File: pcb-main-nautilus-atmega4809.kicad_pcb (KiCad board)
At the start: 4 copper layers, 68.6 x 53.3 mm, 91 parts, among them J1 694106301002, J2 105017-0001, J3 FTSH-105-01-L-DV-007-K, J4 75844-101-06LF, J5 66951-006LF, J6 66951-010LF, J7 66951-008LF, J8 66951-008LF, Q1 BSS138PW, Q2 BSS138PW, Q3 BSS138PW, SW1 PTS645SH43SMTR92 LFS, U1 NCP1117-5.0_TO252, U2 AP2112K-3.3, U3 ATSAMD11D14A-SS, U4 ATmega4809-A

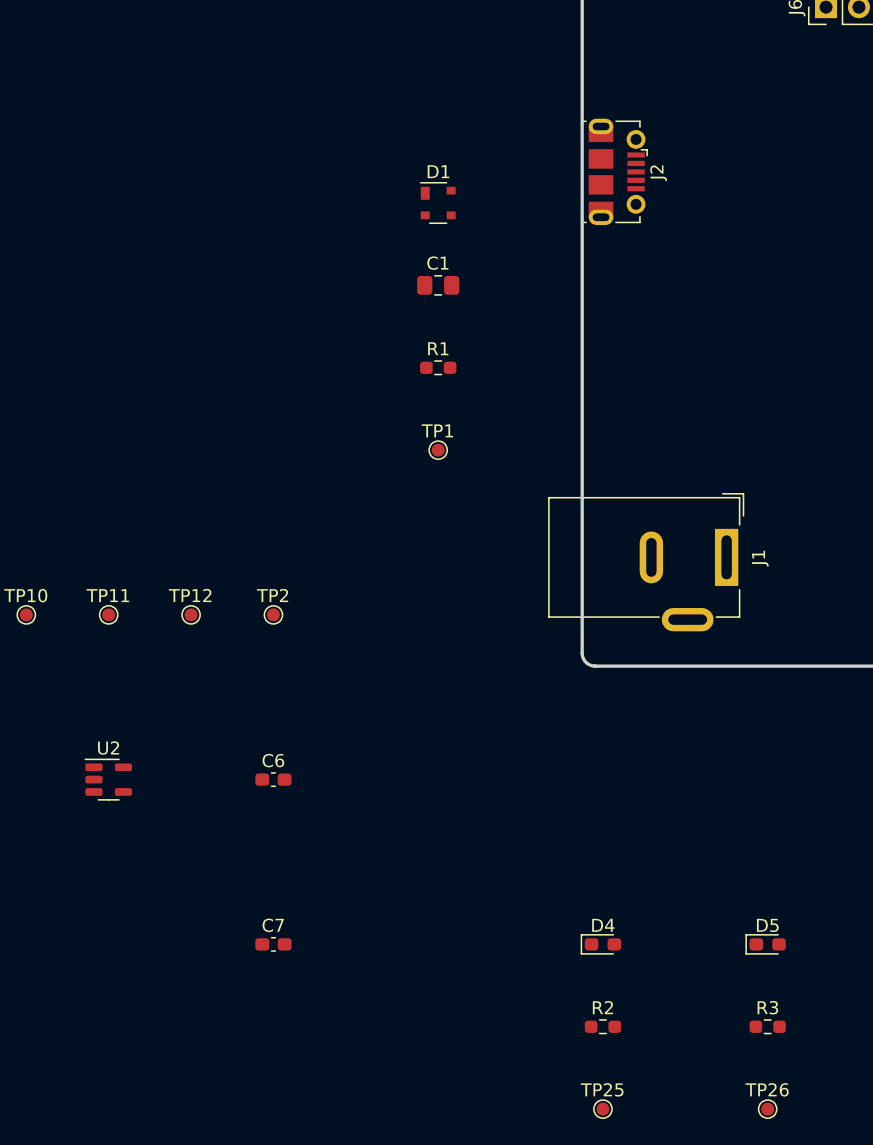
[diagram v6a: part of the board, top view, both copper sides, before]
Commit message: Arrange power indicators
Supports #4.
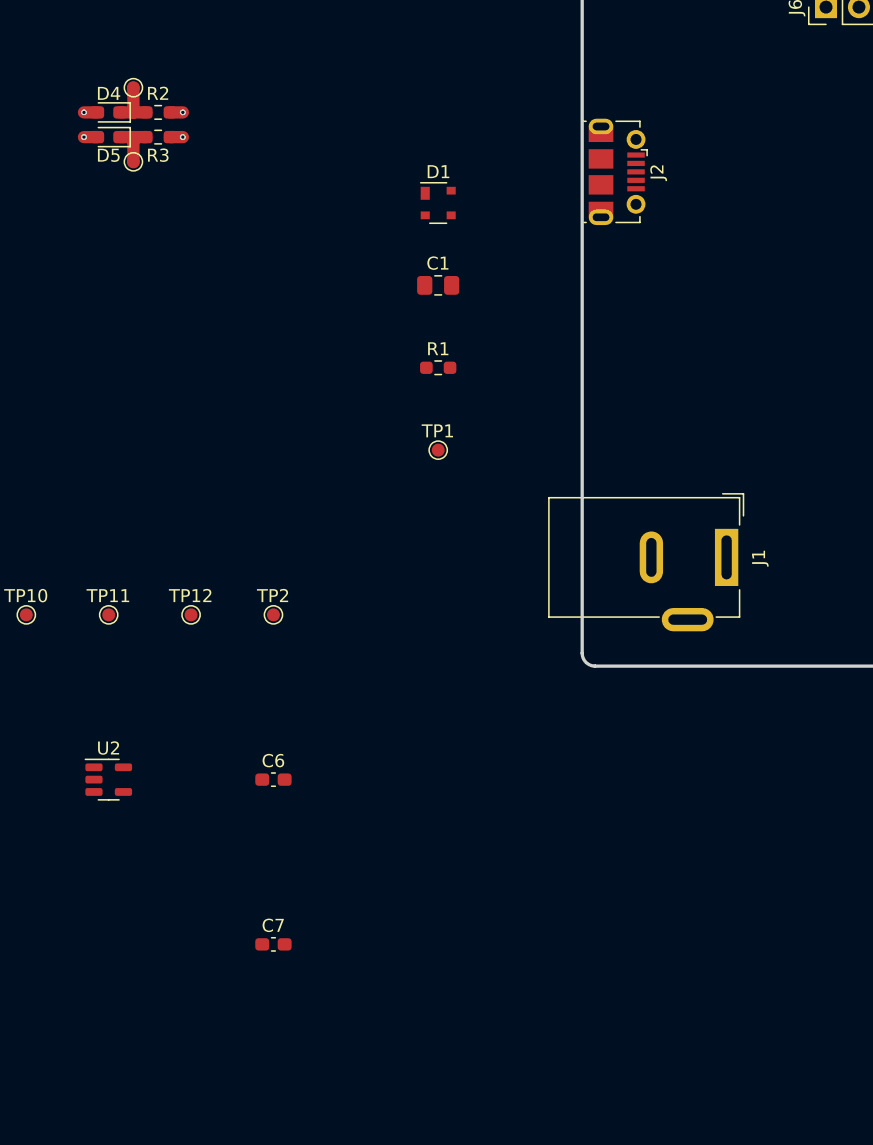
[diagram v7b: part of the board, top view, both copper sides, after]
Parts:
- moved TP26 87.9 mm to (65.4, 111.1)
- moved TP25 86.7 mm to (65.4, 105.4)
- moved R3 83.1 mm to (67.3, 109.2)
- moved D5 80.3 mm to (63.5, 109.2), turned to 180 degrees
- moved R2 78.4 mm to (67.3, 107.3)
- moved D4 74.6 mm to (63.5, 107.3), turned to 180 degrees
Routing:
- net Net-(D5-Pad1): track 0.00 -> 3.93 mm
- net Net-(D4-Pad1): track 0.00 -> 3.93 mm
- net /GND: track 23.7 -> 25.7 mm, vias 8 -> 10
- net /5V: track 15.8 -> 16.8 mm, vias 7 -> 8
- net /3.3V: track 14.8 -> 15.8 mm, vias 7 -> 8
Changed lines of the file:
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@@
   )
   (footprint "LED_SMD:LED_0603_1608Metric_Pad1.05x0.95mm_HandSolder" (layer "F.Cu")
-    (at 101.6 171.45)
+    (at 63.5 107.315 180)
     (descr "LED SMD 0603 (1608 Metric), square (rectangular) end terminal, IPC_7351 nominal, (Body size source: http://www.tortai-tech.com/upload/download/2011102023233369053.pdf), generated with kicad-footprint-generator")
     (tags "LED handsolder")
@@
     (property "Sheetname" "POWER")
     (attr smd)
-    (fp_text reference "D4" (at 0 -1.43) (layer "F.SilkS")
+    (fp_text reference "D4" (at 0 1.43) (layer "F.SilkS")
       (effects (font (size 1 1) (thickness 0.15)))
     )
@@
     (fp_line (start -0.8 0.4) (end 0.8 0.4) (layer "F.Fab") (width 0.1))
     (fp_line (start 0.8 0.4) (end 0.8 -0.4) (layer "F.Fab") (width 0.1))
-    (pad "1" smd roundrect (at -0.875 0) (size 1.05 0.95) (layers "F.Cu" "F.Paste" "F.Mask") (roundrect_rratio 0.25)
+    (pad "1" smd roundrect (at -0.875 0 180) (size 1.05 0.95) (layers "F.Cu" "F.Paste" "F.Mask") (roundrect_rratio 0.25)
       (net 13 "Net-(D4-Pad1)") (pinfunction "K") (pintype "passive"))
-    (pad "2" smd roundrect (at 0.875 0) (size 1.05 0.95) (layers "F.Cu" "F.Paste" "F.Mask") (roundrect_rratio 0.25)
+    (pad "2" smd roundrect (at 0.875 0 180) (size 1.05 0.95) (layers "F.Cu" "F.Paste" "F.Mask") (roundrect_rratio 0.25)
       (net 4 "/5V") (pinfunction "A") (pintype "passive"))
     (model "${KICAD6_3DMODEL_DIR}/LED_SMD.3dshapes/LED_0603_1608Metric.wrl"
@@
   )
   (footprint "TestPoint:TestPoint_Pad_D1.0mm" (layer "F.Cu")
-    (at 114.3 184.15)
+    (at 65.405 111.125)
     (descr "SMD pad as test Point, diameter 1.0mm")
     (tags "test point SMD pad")
@@
     (property "Sheetname" "POWER")
     (attr exclude_from_pos_files)
-    (fp_text reference "TP26" (at 0 -1.448) (layer "F.SilkS")
+    (fp_text reference "TP26" (at 0 -1.448) (layer "F.SilkS") hide
       (effects (font (size 1 1) (thickness 0.15)))
     )
@@
   )
   (footprint "Resistor_SMD:R_0603_1608Metric_Pad0.98x0.95mm_HandSolder" (layer "F.Cu")
-    (at 114.3 177.8)
+    (at 67.31 109.22)
     (descr "Resistor SMD 0603 (1608 Metric), square (rectangular) end terminal, IPC_7351 nominal with elongated pad for handsoldering. (Body size source: IPC-SM-782 page 72, https://www.pcb-3d.com/wordpress/wp-content/uploads/ipc-sm-782a_amendment_1_and_2.pdf), generated with kicad-footprint-generator")
     (tags "resistor handsolder")
@@
     (property "Sheetname" "POWER")
     (attr smd)
-    (fp_text reference "R3" (at 0 -1.43) (layer "F.SilkS")
+    (fp_text reference "R3" (at 0 1.43) (layer "F.SilkS")
       (effects (font (size 1 1) (thickness 0.15)))
     )
@@
   )
   (footprint "Resistor_SMD:R_0603_1608Metric_Pad0.98x0.95mm_HandSolder" (layer "F.Cu")
-    (at 101.6 177.8)
+    (at 67.31 107.315)
     (descr "Resistor SMD 0603 (1608 Metric), square (rectangular) end terminal, IPC_7351 nominal with elongated pad for handsoldering. (Body size source: IPC-SM-782 page 72, https://www.pcb-3d.com/wordpress/wp-content/uploads/ipc-sm-782a_amendment_1_and_2.pdf), generated with kicad-footprint-generator")
     (tags "resistor handsolder")
@@
   )
   (footprint "TestPoint:TestPoint_Pad_D1.0mm" (layer "F.Cu")
-    (at 101.6 184.15)
+    (at 65.405 105.41)
     (descr "SMD pad as test Point, diameter 1.0mm")
     (tags "test point SMD pad")
@@
     (property "Sheetname" "POWER")
     (attr exclude_from_pos_files)
-    (fp_text reference "TP25" (at 0 -1.448) (layer "F.SilkS")
+    (fp_text reference "TP25" (at 0 -1.448) (layer "F.SilkS") hide
       (effects (font (size 1 1) (thickness 0.15)))
     )
@@
   )
   (footprint "LED_SMD:LED_0603_1608Metric_Pad1.05x0.95mm_HandSolder" (layer "F.Cu")
-    (at 114.3 171.45)
+    (at 63.5 109.22 180)
     (descr "LED SMD 0603 (1608 Metric), square (rectangular) end terminal, IPC_7351 nominal, (Body size source: http://www.tortai-tech.com/upload/download/2011102023233369053.pdf), generated with kicad-footprint-generator")
     (tags "LED handsolder")
@@
     (fp_line (start -0.8 -0.1) (end -0.8 0.4) (layer "F.Fab") (width 0.1))
     (fp_line (start -0.8 0.4) (end 0.8 0.4) (layer "F.Fab") (width 0.1))
-    (pad "1" smd roundrect (at -0.875 0) (size 1.05 0.95) (layers "F.Cu" "F.Paste" "F.Mask") (roundrect_rratio 0.25)
+    (pad "1" smd roundrect (at -0.875 0 180) (size 1.05 0.95) (layers "F.Cu" "F.Paste" "F.Mask") (roundrect_rratio 0.25)
       (net 14 "Net-(D5-Pad1)") (pinfunction "K") (pintype "passive"))
-    (pad "2" smd roundrect (at 0.875 0) (size 1.05 0.95) (layers "F.Cu" "F.Paste" "F.Mask") (roundrect_rratio 0.25)
+    (pad "2" smd roundrect (at 0.875 0 180) (size 1.05 0.95) (layers "F.Cu" "F.Paste" "F.Mask") (roundrect_rratio 0.25)
       (net 5 "/3.3V") (pinfunction "A") (pintype "passive"))
     (model "${KICAD6_3DMODEL_DIR}/LED_SMD.3dshapes/LED_0603_1608Metric.wrl"
@@
   (segment (start 195.1 100.9875) (end 195.7125 101.6) (width 0.3) (layer "F.Cu") (net 2))
   (segment (start 195.1 99.4125) (end 195.1 100.9875) (width 0.3) (layer "F.Cu") (net 2))
+  (segment (start 68.2225 109.22) (end 69.215 109.22) (width 0.95) (layer "F.Cu") (net 2))
   (segment (start 110.49 74.93) (end 109.22 74.93) (width 0.95) (layer "F.Cu") (net 2))
   (segment (start 144.04 75.565) (end 142.24 75.565) (width 0.75) (layer "F.Cu") (net 2))
@@
   (segment (start 115.57 78.74) (end 114.3 78.74) (width 1) (layer "F.Cu") (net 2))
   (segment (start 111.5325 74.93) (end 110.49 74.93) (width 0.95) (layer "F.Cu") (net 2))
+  (segment (start 68.2225 107.315) (end 69.215 107.315) (width 0.95) (layer "F.Cu") (net 2))
   (segment (start 201.0125 96) (end 202.5875 96) (width 0.3) (layer "F.Cu") (net 2))
   (segment (start 202.5875 96) (end 203.2 95.3875) (width 0.3) (layer "F.Cu") (net 2))
@@
   (via (at 203.2 93.98) (size 0.4572) (drill 0.254) (layers "F.Cu" "B.Cu") (net 2))
   (via (at 142.24 74.93) (size 0.4572) (drill 0.254) (layers "F.Cu" "B.Cu") (net 2))
+  (via (at 69.215 107.315) (size 0.4572) (drill 0.254) (layers "F.Cu" "B.Cu") (net 2))
   (via (at 110.49 74.93) (size 0.4572) (drill 0.254) (layers "F.Cu" "B.Cu") (net 2))
+  (via (at 69.215 109.22) (size 0.4572) (drill 0.254) (layers "F.Cu" "B.Cu") (net 2))
   (via (at 136.98 79.83) (size 0.4572) (drill 0.254) (layers "F.Cu" "B.Cu") (net 2))
   (via (at 194.945 88.9) (size 0.4572) (drill 0.254) (layers "F.Cu" "B.Cu") (net 2))
@@
   (segment (start 197.1 89.5125) (end 197.7125 88.9) (width 0.3) (layer "F.Cu") (net 4))
   (segment (start 201.0125 96.5) (end 202.5875 96.5) (width 0.3) (layer "F.Cu") (net 4))
+  (segment (start 62.625 107.315) (end 61.595 107.315) (width 0.95) (layer "F.Cu") (net 4))
   (segment (start 115.6825 55.325) (end 114.38 55.325) (width 0.95) (layer "F.Cu") (net 4))
   (segment (start 197.1 91.0875) (end 197.1 89.5125) (width 0.3) (layer "F.Cu") (net 4))
@@
   (via (at 110.49 78.74) (size 0.4572) (drill 0.254) (layers "F.Cu" "B.Cu") (net 4))
   (via (at 114.38 55.325) (size 0.4572) (drill 0.254) (layers "F.Cu" "B.Cu") (net 4))
+  (via (at 61.595 107.315) (size 0.4572) (drill 0.254) (layers "F.Cu" "B.Cu") (net 4))
   (via (at 114.38 59.77) (size 0.4572) (drill 0.254) (layers "F.Cu" "B.Cu") (net 4))
+  (segment (start 62.625 109.22) (end 61.595 109.22) (width 0.95) (layer "F.Cu") (net 5))
   (segment (start 109.87 65.39) (end 109.37 65.39) (width 0.45) (layer "F.Cu") (net 5))
   (segment (start 109.37 56.5) (end 109.1075 56.2375) (width 0.45) (layer "F.Cu") (net 5))
@@
   (segment (start 144.04 73.025) (end 142.24 73.025) (width 0.75) (layer "F.Cu") (net 5))
   (via (at 109.87 65.39) (size 0.4572) (drill 0.254) (layers "F.Cu" "B.Cu") (net 5))
+  (via (at 61.595 109.22) (size 0.4572) (drill 0.254) (layers "F.Cu" "B.Cu") (net 5))
   (via (at 142.24 73.025) (size 0.4572) (drill 0.254) (layers "F.Cu" "B.Cu") (net 5))
   (via (at 134.8475 67.7175) (size 0.4572) (drill 0.254) (layers "F.Cu" "B.Cu") (net 5))
@@
   (segment (start 131.65 75.565) (end 131.65 77.04) (width 0.6) (layer "F.Cu") (net 6))
   (segment (start 135.89 78.105) (end 133.985 78.105) (width 0.95) (layer "F.Cu") (net 6))
+  (segment (start 65.405 107.315) (end 66.3975 107.315) (width 0.95) (layer "F.Cu") (net 13))
+  (segment (start 65.405 107.315) (end 65.405 105.41) (width 0.95) (layer "F.Cu") (net 13))
+  (segment (start 64.375 107.315) (end 65.405 107.315) (width 0.95) (layer "F.Cu") (net 13))
+  (segment (start 65.405 109.22) (end 66.3975 109.22) (width 0.95) (layer "F.Cu") (net 14))
+  (segment (start 64.375 109.22) (end 65.405 109.22) (width 0.95) (layer "F.Cu") (net 14))
+  (segment (start 65.405 109.22) (end 65.405 111.125) (width 0.95) (layer "F.Cu") (net 14))
   (segment (start 137.795 73.025) (end 137.795 71.625) (width 0.6) (layer "F.Cu") (net 20))
   (segment (start 137.795 73.025) (end 140.44 73.025) (width 0.6) (layer "F.Cu") (net 20))
